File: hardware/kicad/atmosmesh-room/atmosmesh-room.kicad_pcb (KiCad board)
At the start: 2 copper layers, 80 x 60 mm, 31 parts, among them U1 IDEASPARK_30PIN_PROVISIONAL

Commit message: :bug: fix(room): make the polarity symbols survive their own gates
The independent review asked for real polarity and C/B/E semantics so ERC can
catch a reversed diode or transistor. Fitting D_Schottky, D and Q_NPN_CBE and
adding per-instance descriptions did that, but left three gates red:

- The local library and the schematic's embedded copy were built from separate
  sources and given different Description text, so all 27 symbols raised
  lib_symbol_mismatch. Both now derive from the one list the schematic embeds,
  which also carries U1's passive pin types across.
- D_BEEP's new anode marker sits 7.62 mm right of the part origin and clipped
  mounting hole H2's mask at x=168. Moved to x=163.
- The .kicad_mod writer indents with spaces, so appending a literal tab to the
  marker continuation lines produced "space before tab" and failed task check.
  Continuation lines now extend the caller's own indent character.

Gates: ERC 0 violations, DRC 0 violations and 0 schematic-parity problems,
structural validation PASS, git diff --check clean. The 52 unconnected items
remain the intentional unrouted ratsnest. generate_project.py reproduces every
artifact byte-identically.
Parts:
- moved D_BEEP 5.00 mm to (163.0, 68.0)

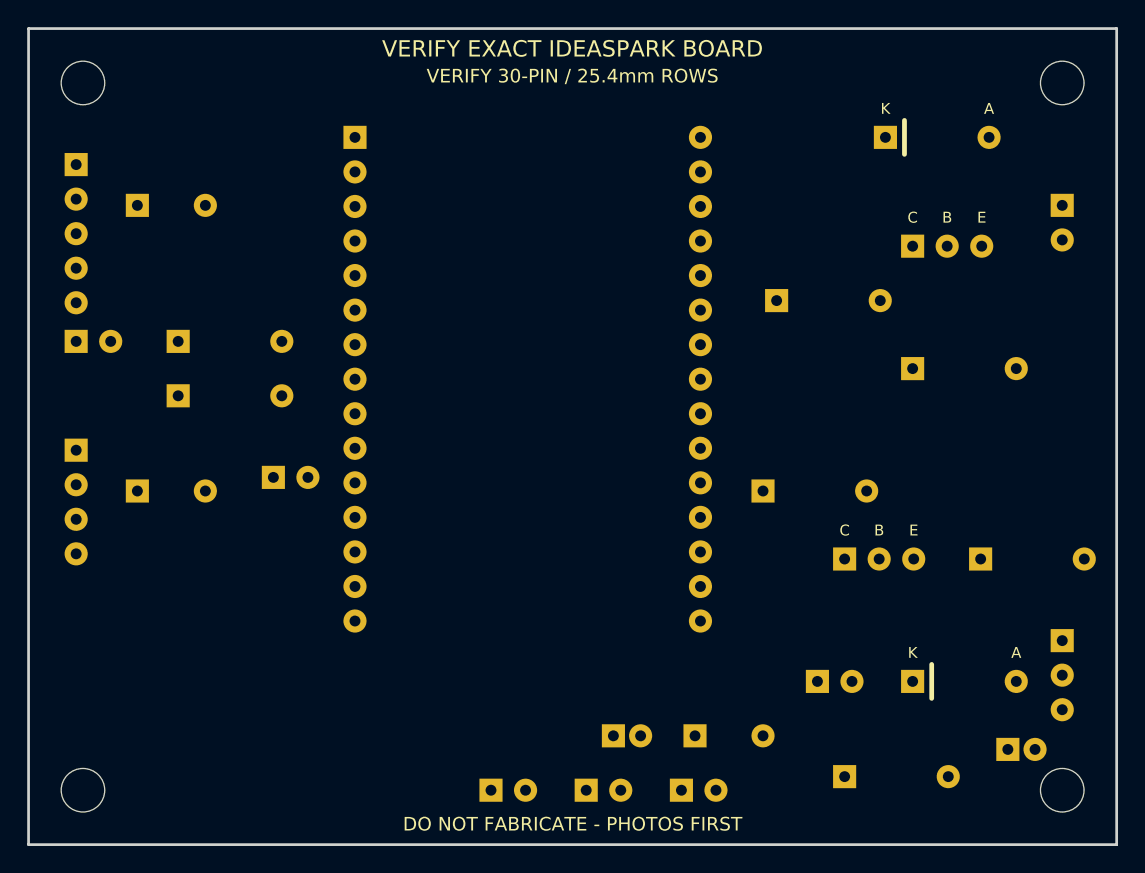
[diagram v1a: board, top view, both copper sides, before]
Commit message: :sparkles: feat(room): build against the board the operator actually has
The controller is the ideaspark ESP32 1.14 inch TFT LCD board, confirmed from
docs/hardware/ideaspark-esp32-tft-pinout.png. The design assumed an integrated
I2C OLED, and that assumption was load-bearing in three places.

Its display is SPI. GPIO21/22 carry no onboard device, so:

- D-022's rejection of a sensor-supply diode rested on the OLED holding SDA/SCL
  at 3.3 V. That reason was false here. The decision is unchanged, on the real
  reason: every pull-up references the same rail the sensors run from.
- Nothing pulls the bus up. D-023 adds R_PU_SDA/R_PU_SCL 4k7 as required parts,
  on the sensor side of the 330R series resistors.
- GPIO23/18/15/2/4/32 belong to the display, GPIO12 is the flash strap and
  GPIO1/3 are the USB-UART. D-024 puts them off-limits behind a generator guard
  and a validator assertion.

U1's socket map was provisional and wrong in almost every position: pad 7 held
GPIO33 where the board has GPIO26, pad 30 held 3V3 where the board has GPIO23.
Rebuilt from a named pin table. Knowing the pin order makes the socket more
dangerous, not less, so the reserved pins are silkscreened too.

Operator also confirmed two module orders that were wrong on the carrier:

- SHT41 is VIN/GND/SCL/SDA; the carrier had SDA and SCL crossed.
- D-SUN PIR is GND/OUT/VCC; the carrier order would have put 5 V on the
  module's ground pin.

Gates: ERC 0, DRC 0 violations and 0 parity problems, structural validation
PASS, git diff --check clean. Both new gates mutation-proved: mapping GPIO23
raises in the generator, a rogue GPIO18 net fails the validator, and dropping
R_PU_SDA fails the pull-up assertion.

Still unverified: the physical row spacing, and both 5 V modules' supply
voltage and output swing.
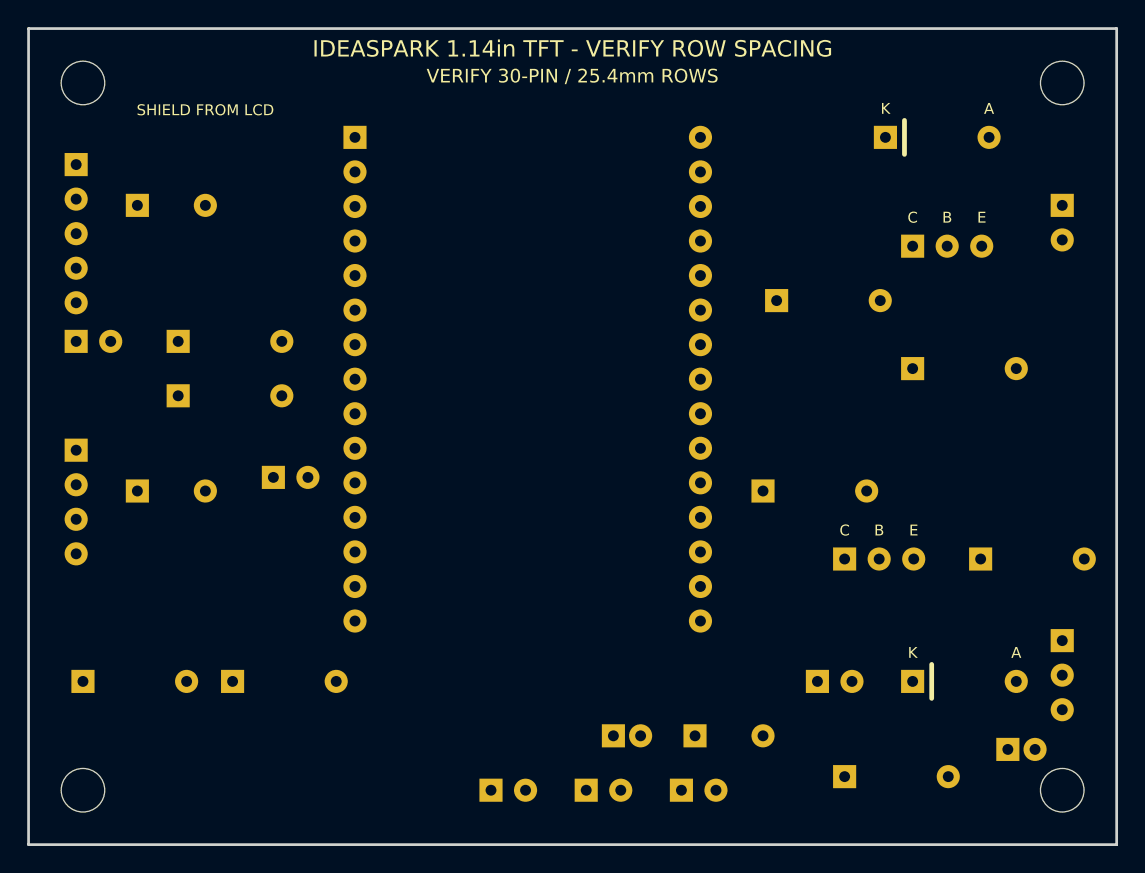
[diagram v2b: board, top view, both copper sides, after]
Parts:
- added R_PU_SCL: 4.7k, room:R_Axial_P7.62mm, F.Cu at (115.0, 108.0)
- added R_PU_SDA: 4.7k, room:R_Axial_P7.62mm, F.Cu at (104.0, 108.0)
- J_PIR: value DSUN_PIR -> DSUN_PIR GND/OUT/VCC
- J_SHT: value SHT41_3V3 -> SHT41 VIN/GND/SCL/SDA
- U1: value IDEASPARK_30PIN_PROVISIONAL -> IDEASPARK_ESP32_1V14_TFT_30PIN
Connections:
- J_PIR pad 1: PIR_5V_PROTECTED -> GND
- J_PIR pad 2: GND -> PIR_OUT
- J_PIR pad 3: PIR_OUT -> PIR_5V_PROTECTED
- J_SHT pad 3: SDA_EXT -> SCL_EXT
- J_SHT pad 4: SCL_EXT -> SDA_EXT
- U1 pad 1: unconnected-(U1-EN-Pad1) -> +5V_USB_CONFIRMED
- U1 pad 14: GND -> unconnected-(U1-GND-Pad14)
- U1 pad 15: +5V_USB_CONFIRMED -> unconnected-(U1-VIN-Pad15)
- U1 pad 16: unconnected-(U1-GPIO23-Pad16) -> +3V3
- U1 pad 17: GPIO22_SCL -> GND
- U1 pad 2: unconnected-(U1-GPIO36/VP-Pad2) -> GND
- U1 pad 20: GPIO21_SDA -> unconnected-(U1-GPIO21-Pad20)
- U1 pad 26: unconnected-(U1-GPIO4-Pad26) -> GPIO21_SDA
- U1 pad 29: GND -> GPIO22_SCL
- U1 pad 30: +3V3 -> unconnected-(U1-3V3-Pad30)
- U1 pad 7: GPIO33_PIR_N -> unconnected-(U1-GPIO33-Pad7)
- U1 pad 9: unconnected-(U1-GPIO26-Pad9) -> GPIO33_PIR_N
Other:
- board text added: "IDEASPARK 1.14in TFT - VERIFY ROW SPACING"
- board text added: "NEVER WIRE: 2 4 15 18 23 32 TFT / 12 STRAP / 1 3 UART"
- board text added: "SHIELD FROM LCD"
- board text removed: "VEML7700 - SHIELD FROM OLED"
- board text removed: "VERIFY EXACT IDEASPARK BOARD"

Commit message: :bug: fix(room): wire the buzzer the module actually has
Operator identified it: a no-name Keyes 3-pin breakout, black cylinder with a
single hole, header order S / VCC / -. It is the same part AtmosMesh v1 uses,
and firmware/README.md records v1 driving it with a bare 50 ms
digitalWrite(HIGH) on GPIO25. So it is an active module with its own driver.

The carrier presented a 2-pin header and switched the load's low side. Against
a 3-pin S/VCC/- module that could not have worked at all: the module's S input
had no connection. Q_BEEP, R_BEEP_IN, R_BEEP_PD and the D_BEEP flyback are
removed. GPIO25 now drives S through R_BEEP_S 100R, active HIGH, matching v1.
No flyback is fitted because an internally-driven module keeps the inductive
kick behind its own transistor.

R_BEEP_S starts at the protective value on purpose. Some Keyes buzzer boards
put the sounder straight across S and - with no onboard transistor, and 100R
would make such a module barely click. The bench rule is to measure rather than
to drive harder: only a measured current under 20 mA authorises a wire link.

ROOM-01's low-side-NPN acceptance criterion is marked superseded rather than
rewritten, and the reasoning is recorded as D-025.

Gates: ERC 0, DRC 0 violations and 0 parity problems, structural validation
PASS, git diff --check clean. The validator now asserts BEEP_BASE and BEEP_LOW
are absent, so the old driver cannot come back unnoticed.
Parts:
- removed D_BEEP: DNP / FIT MAGNETIC ONLY, room:D_Axial_P7.62mm
- removed Q_BEEP: 2N2222_OR_S8050 C/B/E, room:TO92_CBE
- removed R_BEEP_IN: 2.2k, room:R_Axial_P7.62mm
- removed R_BEEP_PD: 100k, room:R_Axial_P7.62mm
- added R_BEEP_S: 100R, room:R_Axial_P7.62mm, F.Cu at (155.0, 80.0)
- J_BEEP: value PIEZO_PROVISIONAL -> KEYES BUZZER S/VCC/-; footprint room:PinHeader_1x02_P2.54mm -> room:PinHeader_1x03_P2.54mm
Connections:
- J_BEEP pad 1: +3V3 -> BEEP_S
- J_BEEP pad 2: BEEP_LOW -> +3V3
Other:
- board text added: "BUZZER S/VCC/-"
- board text removed: "DNP PIEZO"
- board text removed: "FIT MAGNETIC ONLY"

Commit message: :sparkles: feat(room): add the SDS011 with the protection the bench fault earned
ROOM-02. The operator asked for the SDS011 that already worked on AtmosMesh v1,
with additional protection. The protection is aimed at a specific, recorded
failure rather than at hazards in general.

On 2026-08-17 this sensor was wired straight through: its push-pull TXD landed
on the ESP32's push-pull TX2 and the two fought on one net for roughly 10 ms in
every second, against a 40 mA absolute maximum. So:

- The UART is crossed. Sensor TXD reaches GPIO16/RX2, GPIO17/TX2 reaches sensor
  RXD, each through 1k. That bounds a driver fight to about 3.3 mA. At 9600 baud
  a bit is 104 us while 1k into a few hundred pF settles in a couple of hundred
  nanoseconds, so it costs nothing in signal terms.
- generate_project.py refuses to emit a straight-through SDS011 UART.

The PIR's 1N5819 idiom deliberately does NOT transfer to this rail. The SDS011
minimum is 4.7 V and a Schottky drops 0.3-0.4 V at fan current, landing under
the minimum before any USB droop is counted. JP_SDS_5V is default-open instead,
isolating at zero volts, and the generator refuses a diode on that rail.

Both guards are mutation-proved: swapping the header's RXD/TXD nets raises, and
adding a Schottky to the rail raises.

Three power facts are assumed and gate closing the jumper, recorded in D-026 and
as unchecked ROOM-02 criteria rather than left silent: VIN may already sit near
4.6-4.7 V behind a VBUS diode, the shared rail is already near 650 mA peak
coincidence without this sensor, and C6 at 10 uF is not shown to meet the
<20 mV ripple specification against a fan.

Gates: ERC 0, DRC 0 violations and 0 parity problems, structural validation
PASS, git diff --check clean.
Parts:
- added C6: 10uF, room:C_Radial_P2.00mm, F.Cu at (126.0, 112.0)
- added C7: 220nF, room:C_Disc_P5.00mm, F.Cu at (131.0, 108.0)
- added JP_SDS_5V: DEFAULT_OPEN, room:Jumper_2_Open_P2.54mm, F.Cu at (120.0, 112.0)
- added J_SDS: SDS011 5V/GND/RXD/TXD, room:PinHeader_1x04_P2.54mm, F.Cu at (168.0, 84.0)
- added R_SDS_RX: 1k, room:R_Axial_P7.62mm, F.Cu at (108.0, 100.0)
- added R_SDS_TX: 1k, room:R_Axial_P7.62mm, F.Cu at (108.0, 103.0)
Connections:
- U1 pad 21: unconnected-(U1-GPIO19-Pad21) -> GPIO16_SDS_RX
- U1 pad 22: unconnected-(U1-GPIO18-Pad22) -> GPIO17_SDS_TX
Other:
- board text added: "SDS011 5V - NO DIODE - UART CROSSED"

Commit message: :sparkles: feat(room): build on the perfboard and with the parts that exist
ROOM-03 and ROOM-04. The operator solders this by hand on a 31x27 perfboard and
does not need the PCB, and the inventory landed in the repo, so several values
that were chosen "because those parts are available" no longer have to be.

Perfboard becomes the build target (D-027):

- perfboard.md carries the grid facts, placement zones, hole budget and build
  order. The 7x9 cm label and the 31x27 hole count are reconciled: the extra
  millimetres are unholed lead-in strips.
- validate_room_perfboard.py gates it. A build plan with no gate is exactly the
  pattern this repo keeps hitting. All five assertions are mutation-proved.
- Step 1 is a dry-fit. 25.4 mm is exactly 10 pitches, so counting holes settles
  the row spacing that has blocked D-024 since the design started.
- The principal new hazard is orientation: the pinout sheet is a top view and
  soldering happens from the copper side, where left and right invert. Two
  connector orders were already found reversed here, so the wiring table is
  authoritative by pin NAME and the validator refuses to let that warning go.
- atmosmesh-room.kicad_pcb is parked, not deleted. It still cross-checks nets
  and silkscreen; it is not a fabrication candidate.

Values, now that stock is known:

- Pull-ups 4.7k -> 3.3k. Rise time binds on hand-wired perfboard: at 100 kHz
  I2C allows 1000 ns and 4.7k against ~200 pF gives 940 ns, on the limit. 3.3k
  gives 660 ns. wiring.md gains a table justifying every resistor; the operator
  holds a full E24 kit, so none of them is a stock compromise.
- C6 10uF -> 470uF. Its ripple limit is 20 mV against a fan and 10 uF was never
  shown to meet it. C5 and C2 -> 100uF. Electrolytics run to 1000 uF.
- Ceramics go the other way: 220nF -> 100nF for C1/C3/C4/C7, because the
  ceramic assortment stops at 100 nF and D-022 already allowed 47-220 nF.
- Closing JP_SDS_5V now has an ordering rule: before USB power, not while l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
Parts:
- C1, C3, C4, C7: value 220nF -> 100nF
- C2: value 10-47uF -> 100uF
- C5: value 10uF -> 100uF
- C6: value 10uF -> 470uF
- R_PU_SCL, R_PU_SDA: value 4.7k -> 3.3k
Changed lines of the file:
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@@
 			(effects (font (size 0.9 0.9) (thickness 0.15)))
 		)
-		(property "Value" "10uF"
-			(at 0 2 0)
-			(layer "F.Fab")
-			(effects (font (size 0.8 0.8) (thickness 0.12)))
-		)
-		(property "Description" "10 uF protected PIR 5V bulk capacitor; observe polarity"
+		(property "Value" "100uF"
+			(at 0 2 0)
+			(layer "F.Fab")
+			(effects (font (size 0.8 0.8) (thickness 0.12)))
+		)
+		(property "Description" "100 uF protected PIR 5V bulk capacitor; observe polarity"
 			(at 0 0 0) (layer "F.Fab") (hide yes)
 			(effects (font (size 1 1)))
@@
 			(effects (font (size 0.9 0.9) (thickness 0.15)))
 		)
-		(property "Value" "4.7k"
-			(at 0 2 0)
-			(layer "F.Fab")
-			(effects (font (size 0.8 0.8) (thickness 0.12)))
-		)
-		(property "Description" "4.7 kilohm SDA_EXT pullup to 3V3; the TFT board has no onboard I2C pullups"
+		(property "Value" "3.3k"
+			(at 0 2 0)
+			(layer "F.Fab")
+			(effects (font (size 0.8 0.8) (thickness 0.12)))
+		)
+		(property "Description" "3.3 kilohm SDA_EXT pullup to 3V3; sized for perfboard wiring capacitance at 100 kHz"
 			(at 0 0 0) (layer "F.Fab") (hide yes)
 			(effects (font (size 1 1)))
@@
 			(effects (font (size 0.9 0.9) (thickness 0.15)))
 		)
-		(property "Value" "4.7k"
-			(at 0 2 0)
-			(layer "F.Fab")
-			(effects (font (size 0.8 0.8) (thickness 0.12)))
-		)
-		(property "Description" "4.7 kilohm SCL_EXT pullup to 3V3; the TFT board has no onboard I2C pullups"
+		(property "Value" "3.3k"
+			(at 0 2 0)
+			(layer "F.Fab")
+			(effects (font (size 0.8 0.8) (thickness 0.12)))
+		)
+		(property "Description" "3.3 kilohm SCL_EXT pullup to 3V3; sized for perfboard wiring capacitance at 100 kHz"
 			(at 0 0 0) (layer "F.Fab") (hide yes)
 			(effects (font (size 1 1)))
@@
 			(effects (font (size 0.9 0.9) (thickness 0.15)))
 		)
-		(property "Value" "220nF"
-			(at 0 2 0)
-			(layer "F.Fab")
-			(effects (font (size 0.8 0.8) (thickness 0.12)))
-		)
-		(property "Description" "220 nF VEML7700 VIN input decoupling; 47-220 nF acceptable"
+		(property "Value" "100nF"
+			(at 0 2 0)
+			(layer "F.Fab")
+			(effects (font (size 0.8 0.8) (thickness 0.12)))
+		)
+		(property "Description" "100 nF VEML7700 VIN input decoupling"
 			(at 0 0 0) (layer "F.Fab") (hide yes)
 			(effects (font (size 1 1)))
@@
 			(effects (font (size 0.9 0.9) (thickness 0.15)))
 		)
-		(property "Value" "220nF"
-			(at 0 2 0)
-			(layer "F.Fab")
-			(effects (font (size 0.8 0.8) (thickness 0.12)))
-		)
-		(property "Description" "220 nF SHT41 3V3 local decoupling; 47-220 nF acceptable"
+		(property "Value" "100nF"
+			(at 0 2 0)
+			(layer "F.Fab")
+			(effects (font (size 0.8 0.8) (thickness 0.12)))
+		)
+		(property "Description" "100 nF SHT41 3V3 local decoupling"
 			(at 0 0 0) (layer "F.Fab") (hide yes)
 			(effects (font (size 1 1)))
@@
 			(effects (font (size 0.9 0.9) (thickness 0.15)))
 		)
-		(property "Value" "10-47uF"
-			(at 0 2 0)
-			(layer "F.Fab")
-			(effects (font (size 0.8 0.8) (thickness 0.12)))
-		)
-		(property "Description" "10-47 uF controller 3V3 bulk capacitor; observe polarity"
+		(property "Value" "100uF"
+			(at 0 2 0)
+			(layer "F.Fab")
+			(effects (font (size 0.8 0.8) (thickness 0.12)))
+		)
+		(property "Description" "100 uF controller 3V3 bulk capacitor; observe polarity"
 			(at 0 0 0) (layer "F.Fab") (hide yes)
 			(effects (font (size 1 1)))
@@
 			(effects (font (size 0.9 0.9) (thickness 0.15)))
 		)
-		(property "Value" "220nF"
-			(at 0 2 0)
-			(layer "F.Fab")
-			(effects (font (size 0.8 0.8) (thickness 0.12)))
-		)
-		(property "Description" "220 nF controller 3V3 local decoupling; 47-220 nF acceptable"
+		(property "Value" "100nF"
+			(at 0 2 0)
+			(layer "F.Fab")
+			(effects (font (size 0.8 0.8) (thickness 0.12)))
+		)
+		(property "Description" "100 nF controller 3V3 local decoupling"
 			(at 0 0 0) (layer "F.Fab") (hide yes)
 			(effects (font (size 1 1)))
@@
 			(effects (font (size 0.9 0.9) (thickness 0.15)))
 		)
-		(property "Value" "10uF"
-			(at 0 2 0)
-			(layer "F.Fab")
-			(effects (font (size 0.8 0.8) (thickness 0.12)))
-		)
-		(property "Description" "10 uF protected SDS011 5V bulk capacitor; observe polarity"
+		(property "Value" "470uF"
+			(at 0 2 0)
+			(layer "F.Fab")
+			(effects (font (size 0.8 0.8) (thickness 0.12)))
+		)
+		(property "Description" "470 uF protected SDS011 5V bulk; sized for the fan against the 20 mV ripple limit; observe polarity"
 			(at 0 0 0) (layer "F.Fab") (hide yes)
 			(effects (font (size 1 1)))
@@
 			(effects (font (size 0.9 0.9) (thickness 0.15)))
 		)
-		(property "Value" "220nF"
-			(at 0 2 0)
-			(layer "F.Fab")
-			(effects (font (size 0.8 0.8) (thickness 0.12)))
-		)
-		(property "Description" "220 nF SDS011 5V high-frequency decoupling"
-			(at 0 0 0) (layer "F.Fab") (hide yes)
-			(effects (font (size 1 1)))
+		(property "Value" "100nF"
+			(at 0 2 0)
+			(layer "F.Fab")
+			(effects (font (size 0.8 0.8) (thickness 0.12)))
+		)
+		(property "Description" "100 nF SDS011 5V high-frequency decoupling"
+			(at 0 0 0) (layer "F.Fab") (hide yes)
+			(effects (font (size 1 1)))
